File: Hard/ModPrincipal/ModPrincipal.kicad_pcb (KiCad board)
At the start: 2 copper layers, 100 x 60 mm, 114 parts, among them J401 Conn_01x05, J402 Conn_01x05, J501 Conn_01x03, J503 Conn_01x02, J601 Conn_02x10_Odd_Even, J602 Conn_02x05_Odd_Even, J801 Conn_01x06, K701 RT42xxxx, Q401 2N7002, Q701 2N7002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

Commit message: Inicio ubicacion de componentes
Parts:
- added H101: MountingHole, MountingHole:MountingHole_3.2mm_M3, F.Cu at (31.0, 44.0)
- added H102: MountingHole, MountingHole:MountingHole_3.2mm_M3, F.Cu at (31.0, 92.0)
- added H103: MountingHole, MountingHole:MountingHole_3.2mm_M3, F.Cu at (124.0, 44.0)
- added H104: MountingHole, MountingHole:MountingHole_3.2mm_M3, F.Cu at (34.0, 130.9)
- moved D702 240.6 mm to (78.8, 18.0)
- moved D703 206.8 mm to (86.4, 22.5)
- moved D706 206.8 mm to (86.4, 25.8)
- moved Q702 206.8 mm to (123.2, 20.6)
- moved Q703 206.8 mm to (118.4, 23.6)
- moved Q704 206.8 mm to (127.9, 17.4)
- moved R701 206.8 mm to (124.9, 10.7)
- moved R715 206.8 mm to (124.9, 7.71)
- moved C701 206.8 mm to (118.6, 19.8)
- moved C702 206.8 mm to (124.1, 13.6)
- moved C703 206.8 mm to (123.3, 16.9)
- moved D704 206.8 mm to (117.4, 7.86)
- moved D705 206.8 mm to (96.8, 22.5)
- moved D707 206.8 mm to (96.8, 25.8)
- moved D708 206.8 mm to (100.3, 18.3)
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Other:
- board size 100 x 60 mm -> 125.5 x 146.5 mm

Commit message: Avance en place de componentes
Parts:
- added R805: R, Resistor_SMD:R_0805_2012Metric_Pad1.15x1.40mm_HandSolder, F.Cu at (45.0, 45.0)
- added R806: R, Resistor_SMD:R_0805_2012Metric_Pad1.15x1.40mm_HandSolder, F.Cu at (45.0, 46.9)
- added R807: R, Resistor_SMD:R_0805_2012Metric_Pad1.15x1.40mm_HandSolder, F.Cu at (45.0, 49.0)
- added R808: R, Resistor_SMD:R_0805_2012Metric_Pad1.15x1.40mm_HandSolder, F.Cu at (45.0, 51.0)
- D703, D704, D705, D706, D707, D708: footprint Diode_SMD:D_MiniMELF_Handsoldering -> Diode_SMD:D_MiniMELF
- K701: value RT42xxxx -> RT44xxxx; footprint Relay_THT:Relay_DPDT_Schrack-RT2-FormC_RM5mm -> Relay_THT:Relay_DPST_Schrack-RT2-FormA_RM5mm
- U801: value BP -> BP2; footprint BluePill:BLUEPILL -> BluePill:BLUEPILL2
- moved R305 276.1 mm to (57.0, 84.1), turned to 180 degrees
- moved R306 276.1 mm to (57.0, 88.0), turned to 180 degrees
- moved TP202 236.5 mm to (74.0, 89.0), turned to 180 degrees
- moved R301 234.2 mm to (103.0, 98.0), turned to 180 degrees
- moved C303 233.6 mm to (99.0, 100.0)
- moved R208 232.0 mm to (79.0, 89.0)
- moved TP201 231.6 mm to (74.0, 101.0), turned to 180 degrees
- moved U302 228.2 mm to (100.0, 106.0), turned to 270 degrees
- moved R207 227.3 mm to (79.0, 101.0)
- moved R204 226.9 mm to (84.0, 89.0)
- moved C301 226.5 mm to (106.0, 105.0), turned to 270 degrees
- moved R304 226.0 mm to (111.0, 98.0), turned to 180 degrees
- moved R302 225.4 mm to (103.0, 100.0), turned to 180 degrees
- moved R206 224.4 mm to (77.0, 93.0), turned to 180 degrees
- moved R203 222.4 mm to (84.0, 101.0)
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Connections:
- K701 pad 11: /IOs digitales/L_220V_Out -> L_220VAC
- K701 pad 14: L_220VAC -> /IOs digitales/L_220V_Out
- K701 pad 21: /IOs digitales/N_220V_Out -> N_220VAC
- K701 pad 24: N_220VAC -> /IOs digitales/N_220V_Out
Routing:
- added copper zone on F.Cu, net +3V3
- added copper zone on F.Cu, net +5V
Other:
- board size 125.5 x 146.5 mm -> 112.5 x 137.5 mm

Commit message: Avance en trazado de pista Modulo principal
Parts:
- removed D502: 1N4007, Diode_THT:D_DO-41_SOD81_P10.16mm_Horizontal
- removed J801: Conn_01x06, Connector_PinHeader_2.54mm:PinHeader_1x06_P2.54mm_Vertical
- added C801: 100nF, Capacitor_SMD:C_0805_2012Metric_Pad1.15x1.40mm_HandSolder, B.Cu at (49.0, 94.0)
- added C802: 100nF, Capacitor_SMD:C_0805_2012Metric_Pad1.15x1.40mm_HandSolder, B.Cu at (51.0, 94.0)
- C205, C206, C505, D501, R801, R802, R803, R804: moved to B.Cu
- J602: footprint Connector_PinSocket_2.54mm:PinSocket_2x05_P2.54mm_Horizontal -> Connector:PinSocket_2x03_Doble_Paso_P2.54mm_Horizontal
- moved D707 95.1 mm to (86.8, 82.5)
- moved C702 91.9 mm to (72.0, 86.0), turned to 270 degrees
- moved D708 91.0 mm to (91.5, 87.2), turned to 270 degrees
- moved R713 87.0 mm to (77.0, 86.0), turned to 270 degrees
- moved R714 86.0 mm to (94.0, 88.0), turned to 270 degrees
- moved D706 84.3 mm to (74.5, 85.2), turned to 270 degrees
- moved D705 83.3 mm to (79.5, 83.2), turned to 270 degrees
- moved R710 82.2 mm to (77.0, 82.0), turned to 90 degrees
- moved C703 81.6 mm to (96.0, 88.0), turned to 270 degrees
- moved R716 80.7 mm to (72.0, 82.5), turned to 90 degrees
- moved R717 76.6 mm to (98.0, 88.0), turned to 270 degrees
- moved R711 76.5 mm to (97.0, 85.0)
- moved D703 58.6 mm to (82.0, 83.2), turned to 270 degrees
- moved D704 57.6 mm to (89.0, 87.2), turned to 270 degrees
- moved R709 57.1 mm to (85.5, 85.0), turned to 0 degrees
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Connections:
- C205 pad 2: GNDA -> GND
- C206 pad 2: GNDA -> GND
- C303 pad 1: +3V3 -> +3.3VA
- C304 pad 1: +3V3 -> +3.3VA
- J503 pad 1: Net-(D501-Pad1) -> Net-(D501-Pad2)
- J503 pad 2: Net-(D501-Pad2) -> Net-(D501-Pad1)
- R305 pad 1: +3V3 -> +3.3VA
- R306 pad 1: +3V3 -> +3.3VA
- R406 pad 1: +3V3 -> +3.3VA
- R407 pad 1: +3V3 -> +3.3VA
- R805 pad 1: +3V3 -> +3.3VA
- R806 pad 1: +3V3 -> +3.3VA
- R807 pad 1: +3V3 -> +3.3VA
- R808 pad 1: +3V3 -> +3.3VA
- U302 pad 3: +3V3 -> +3.3VA
- U801 pad 3V3: Net-(U801-Pad3V3) -> +3.3VA
- U801 pad PA2: /IOs digitales/CPU_ModPower -> /IOs digitales/CPU_Out0
- U801 pad PA3: /IOs digitales/CPU_Out0 -> /IOs digitales/CPU_Out1
- U801 pad PA4: /IOs digitales/CPU_Out1 -> /IOs digitales/CPU_Out2
- U801 pad PA5: /IOs digitales/CPU_Out2 -> /IOs digitales/CPU_ModPower
- U801 pad PB3: /IOs digitales/CPU_In0 -> /IOs digitales/CPU_In2
- U801 pad PB5: /IOs digitales/CPU_In2 -> /IOs digitales/CPU_In0
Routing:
- net +5V: track 0.00 -> 166.4 mm, vias 0 -> 4
- net +12V: track 0.00 -> 64.7 mm
- net +3V3: track 0.00 -> 63.9 mm
- net /IOs digitales/CPU_Out2: track 0.00 -> 62.1 mm, vias 0 -> 1
- net /IOs digitales/CPU_Out1: track 0.00 -> 58.5 mm, vias 0 -> 1
- net /IOs digitales/CPU_Out0: track 0.00 -> 57.1 mm
- net /IOs digitales/CPU_In0: track 0.00 -> 56.5 mm
- net /IOs digitales/Entrada2: track 0.00 -> 46.2 mm, vias 0 -> 2
- net /IOs digitales/CPU_In1: track 0.00 -> 42.1 mm
- net /IOs digitales/Entrada1: track 0.00 -> 41.2 mm
- net L_220VAC: track 0.00 -> 40.0 mm
- net /AnalogInputs/ADC0: track 0.00 -> 39.1 mm
- net /AnalogInputs/ADC1: track 0.00 -> 36.8 mm
- net GND: track 0.00 -> 33.9 mm, vias 0 -> 1
- net /IOs digitales/Entrada0: track 0.00 -> 33.2 mm
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- added copper zone on F.Cu, net +12V
- added copper zone on B.Cu, net GND
- added copper zone on F.Cu, net GND
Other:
- net class 220 added: clearance 2, trace_width 2, via_dia 2, via_drill 1
- net class Default: clearance 0.2 -> 0.5; trace_width 0.25 -> 0.5; via_dia 0.8 -> 1.5; via_drill 0.4 -> 0.7
- net class IOs added: clearance 0.25, trace_width 0.5, via_dia 1.5, via_drill 0.7
- rule trace_clearance: 0.2 -> 0.5
- board text added: "Clearance: -U302 local clearance 0.3mm"

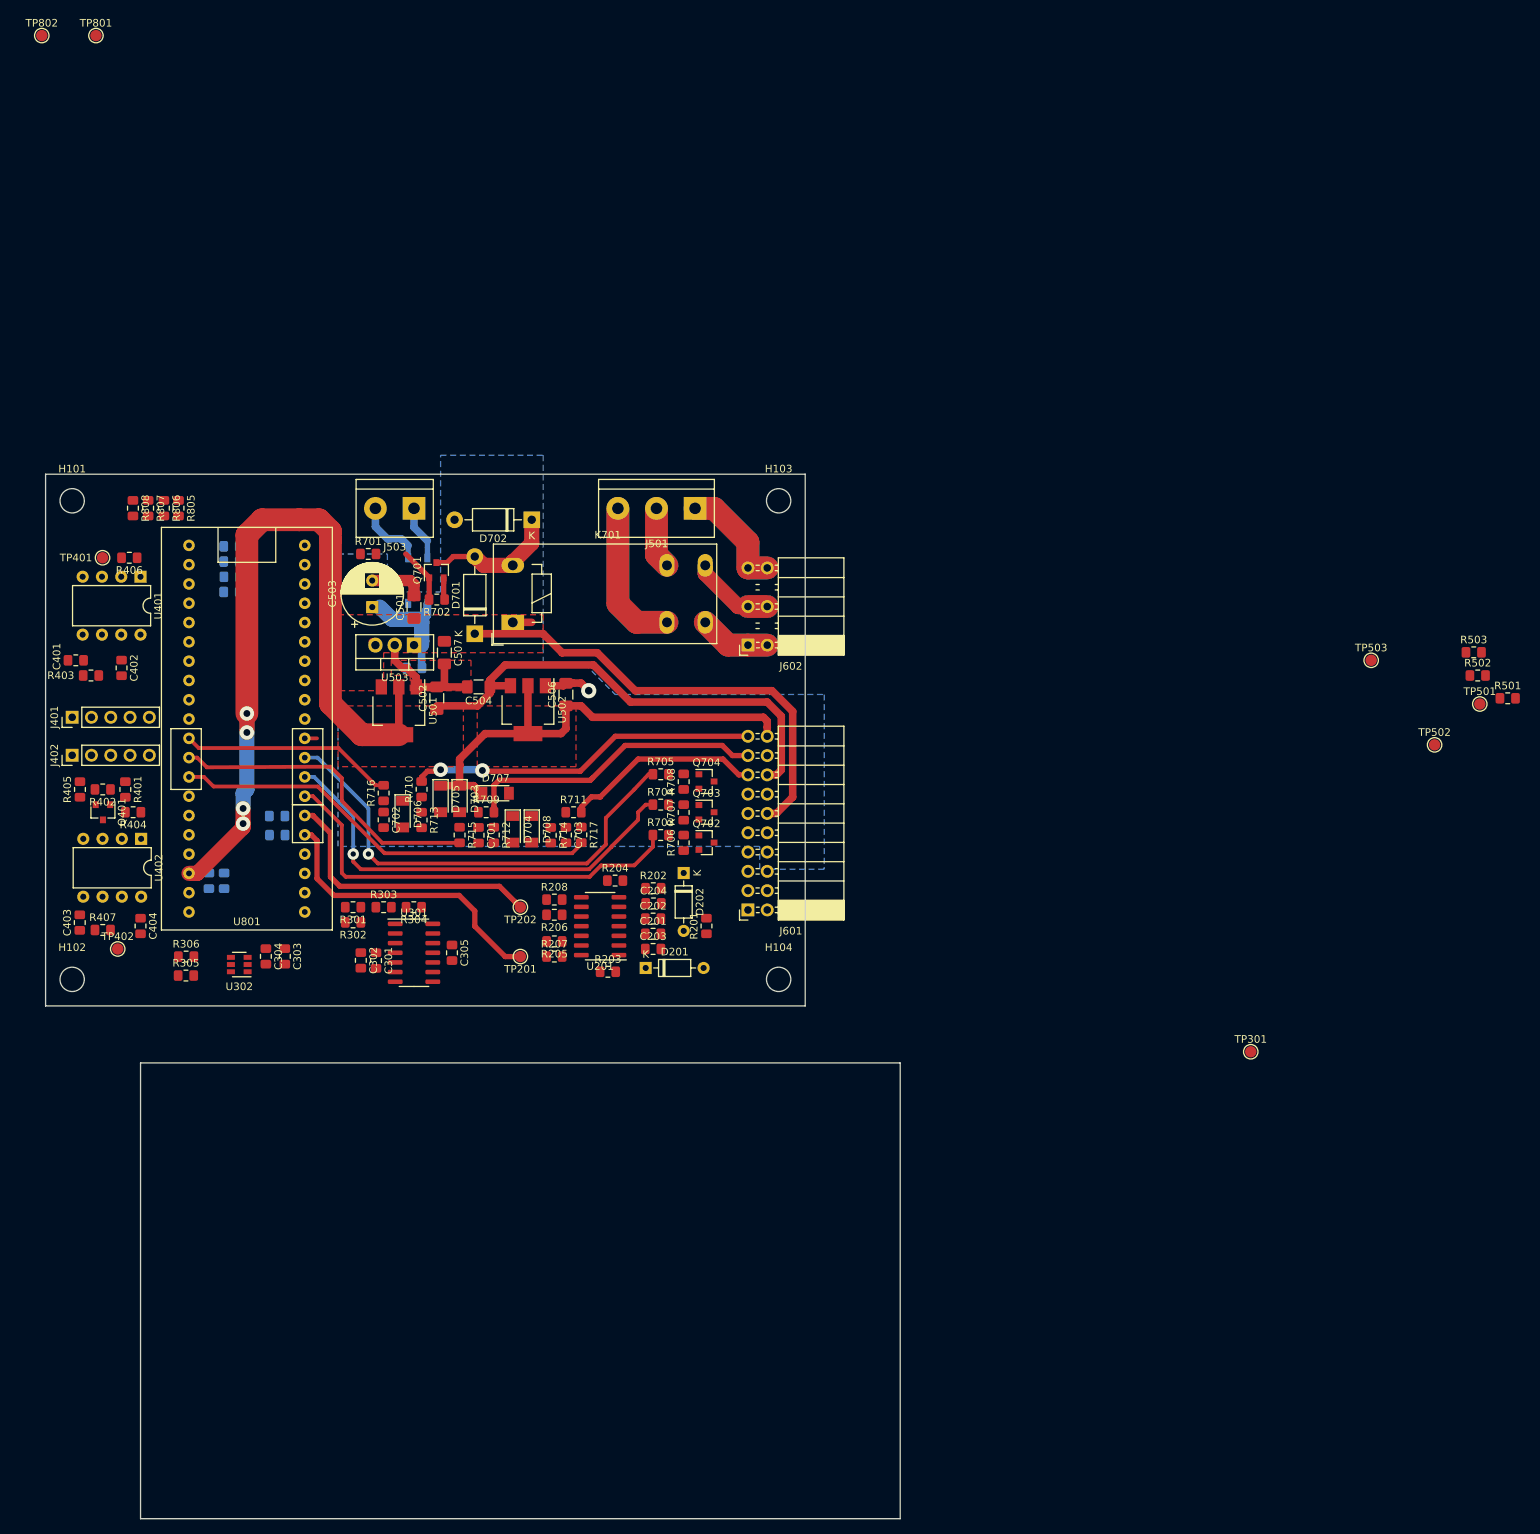
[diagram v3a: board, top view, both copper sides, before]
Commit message: Trazado completo de PCB modulo principal V1.0
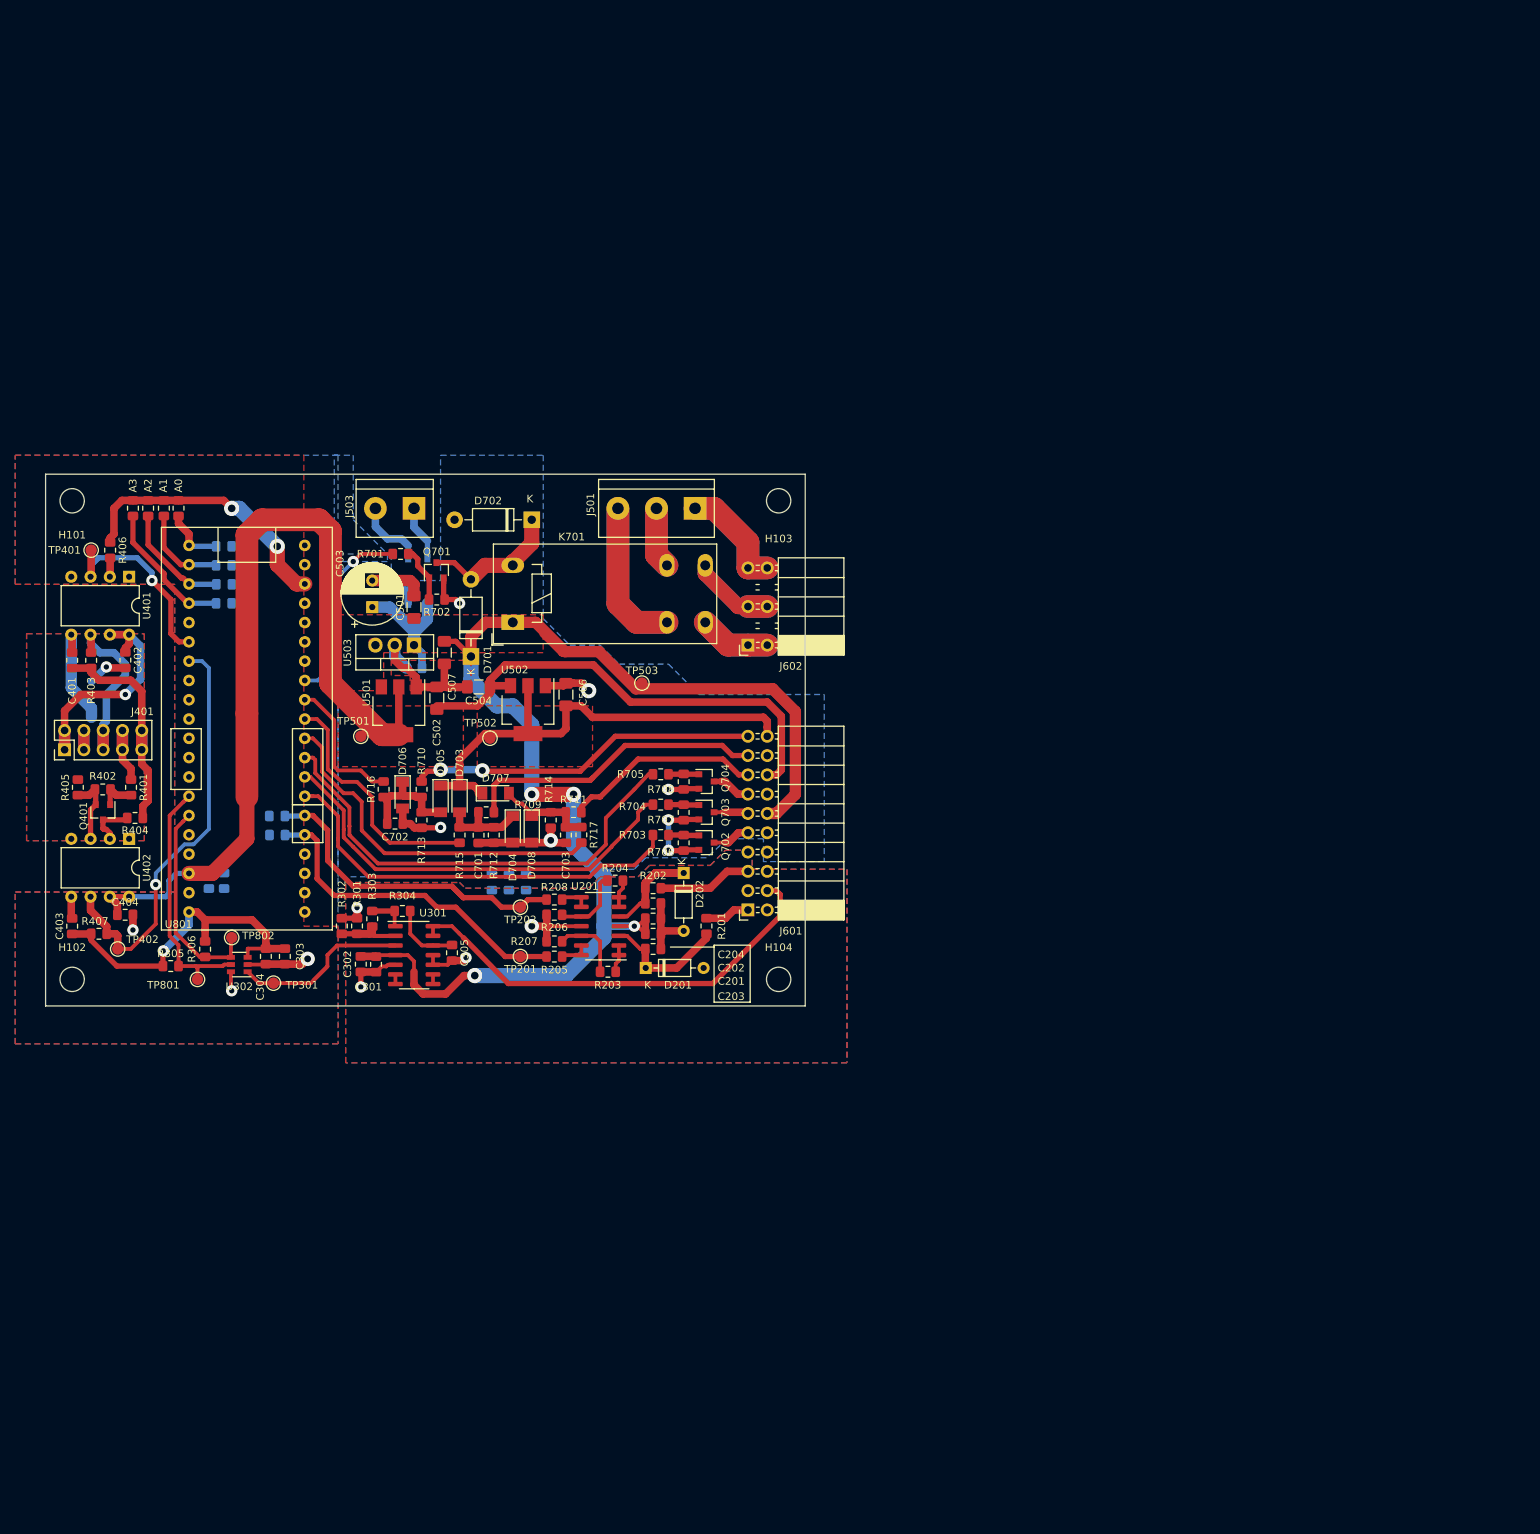
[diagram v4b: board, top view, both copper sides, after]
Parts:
- removed J402: Conn_01x05, Connector_PinHeader_2.54mm:PinHeader_1x05_P2.54mm_Vertical
- J401: value Conn_01x05 -> Conn_02x05_Odd_Even; footprint Connector_PinHeader_2.54mm:PinHeader_1x05_P2.54mm_Vertical -> Connector_PinHeader_2.54mm:PinHeader_2x05_P2.54mm_Vertical
- R501, R502, R503: moved to B.Cu
- moved TP501 147.4 mm to (69.0, 75.0)
- moved R501 135.9 mm to (86.2, 94.2), turned to 90 degrees
- moved R502 130.4 mm to (88.5, 94.2), turned to 90 degrees
- moved TP301 129.0 mm to (57.5, 107.5)
- moved R503 128.4 mm to (90.8, 94.2), turned to 90 degrees
- moved TP801 125.0 mm to (47.5, 107.0)
- moved TP502 124.4 mm to (86.0, 75.2)
- moved TP802 121.3 mm to (52.0, 101.5)
- moved TP503 96.0 mm to (106.0, 68.0)
- moved J401 4.39 mm to (30.0, 76.8)
- moved R701 4.25 mm to (74.2, 51.0)
- moved D701 3.04 mm to (83.5, 64.5)
- moved R406 2.72 mm to (36.0, 50.5), turned to 270 degrees
- moved R306 2.68 mm to (48.5, 103.0), turned to 270 degrees
- moved R301 2.53 mm to (68.5, 100.0), turned to 90 degrees
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- renumbered R805 to A0, R806 to A1, R807 to A2, R808 to A3
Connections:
- C403 pad 1: +3V3 -> +3.3VA
- J401 pad 2: GNDS -> +5VP
- J401 pad 3: /UARTAislada/UARTMaster_Rx -> GNDS
- J401 pad 4: /UARTAislada/UARTMaster_Tx -> GNDS
- J401 pad 5: +3.3VP -> /UARTAislada/UARTMaster_Rx
- U801 pad PA5: /IOs digitales/CPU_ModPower -> /IOs digitales/CPU_In0
- U801 pad PA6: Net-(J801-Pad5) -> /IOs digitales/CPU_In1
- U801 pad PA7: Net-(J801-Pad4) -> /IOs digitales/CPU_In2
- U801 pad PB0: Net-(J801-Pad3) -> /IOs digitales/CPU_ModPower
- U801 pad PB3: /IOs digitales/CPU_In2 -> Net-(U801-PadPB3)
- U801 pad PB4: /IOs digitales/CPU_In1 -> Net-(U801-PadPB4)
- U801 pad PB5: /IOs digitales/CPU_In0 -> Net-(U801-PadPB5)
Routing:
- net +12V: track 64.7 -> 189.7 mm, vias 0 -> 4
- net +3.3VA: track 0.00 -> 81.0 mm, vias 0 -> 3
- net GND: track 33.9 -> 99.3 mm, vias 1 -> 10
- net /AnalogOut/AnalogOut: track 0.00 -> 58.6 mm
- net /UARTAislada/UARTSlave_RX: track 0.00 -> 55.7 mm, vias 0 -> 1
- net GNDA: track 0.00 -> 39.0 mm, vias 0 -> 4
- net /AnalogOut/SCL: track 0.00 -> 33.8 mm
- net +5VP: track 0.00 -> 31.0 mm, vias 0 -> 1
- net +3.3VP: track 0.00 -> 30.6 mm
- net /AnalogOut/SDA: track 0.00 -> 27.4 mm
- net /UARTAislada/UARTSlave_TX: track 0.00 -> 26.2 mm, vias 0 -> 1
- net Net-(TP301-Pad1): track 0.00 -> 25.6 mm
- net GNDS: track 0.00 -> 24.8 mm, vias 0 -> 1
- net /UARTAislada/UARTMaster_Rx: track 0.00 -> 24.3 mm
- net /IOs digitales/CPU_ModPower: track 1.61 -> 24.9 mm, vias 0 -> 1
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- added copper zone on B.Cu, net GNDA
- added copper zone on F.Cu, net GNDA
- added copper zone on B.Cu, net GNDS
- added copper zone on F.Cu, net GNDS
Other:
- board size 112.5 x 137.5 mm -> 100 x 70 mm
- net class DAC added: clearance 0.3, trace_width 0.5, via_dia 1.5, via_drill 0.7
- board text added: "Clearance: -U302 local clearance 0.3mm -Señales IOs, UART y DAC 0.3"
- board text removed: "Clearance: -U302 local clearance 0.3mm"

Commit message: Primera correccion en modulos Adicionales y cambio de etapa de salida en modulo principal
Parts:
- removed Q702, Q703, Q704: 2N7002, Package_TO_SOT_SMD:SOT-23
- removed R706, R707, R708: 330 k, Resistor_SMD:R_0805_2012Metric_Pad1.15x1.40mm_HandSolder
- added U701: PC817, Package_SO:SO-4_7.6x3.6mm_P2.54mm, F.Cu at (110.5, 90.0)
- added U702: PC817, Package_SO:SO-4_7.6x3.6mm_P2.54mm, F.Cu at (110.5, 85.0)
- added U703: PC817, Package_SO:SO-4_7.6x3.6mm_P2.54mm, F.Cu at (110.0, 80.0)
- R703, R704, R705: value 10k -> 330
- moved R705 9.01 mm to (101.0, 85.0), turned to 90 degrees
- moved R703 5.84 mm to (103.0, 90.0), turned to 90 degrees
- moved R704 5.57 mm to (103.0, 85.0), turned to 90 degrees
- moved D202 0.50 mm to (111.5, 93.5)
- renumbered A0 to R805, A1 to R806, A2 to R807, A3 to R808
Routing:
- net GND: track 99.3 -> 131.3 mm, vias 10 -> 9
- net /IOs digitales/CPU_Out2: track 61.7 -> 52.7 mm
- net /IOs digitales/CPU_Out0: track 56.8 -> 50.8 mm
- net /IOs digitales/Entrada0: track 33.2 -> 28.5 mm
- net /IOs digitales/CPU_Out1: track 57.2 -> 53.0 mm
- net Net-(R705-Pad2): track 4.04 -> 7.63 mm
- net Net-(C204-Pad1): track 18.0 -> 14.5 mm
- net /Puerto/Out_Digital2: track 5.15 -> 7.23 mm
- net Net-(R704-Pad2): track 4.02 -> 2.86 mm
- net Net-(R703-Pad2): track 4.02 -> 2.86 mm
- net /AnalogInputs/Analog1: track 12.4 -> 13.2 mm
- net /Puerto/Out_Digital1: track 4.53 -> 5.31 mm

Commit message: Inicio placement de componentes en Modulos Adicionales
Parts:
- J501: footprint TerminalBlock:TerminalBlock_bornier-3_P5.08mm -> Conectores:TerminalBlock_bornier-3_P5.00mm
- J503: footprint TerminalBlock:TerminalBlock_bornier-2_P5.08mm -> Conectores:TerminalBlock_bornier-2_P5.00mm
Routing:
- net L_220VAC: track 40.0 -> 42.4 mm

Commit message: Primera version de PCBs para fabricar
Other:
- board text added: "CESE-FIUBA"
- board text added: "Gonzalo Gontad"
